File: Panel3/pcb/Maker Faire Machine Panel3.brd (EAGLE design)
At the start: 101.6 x 87.6 mm, 40 parts, among them IC1 TJA1049

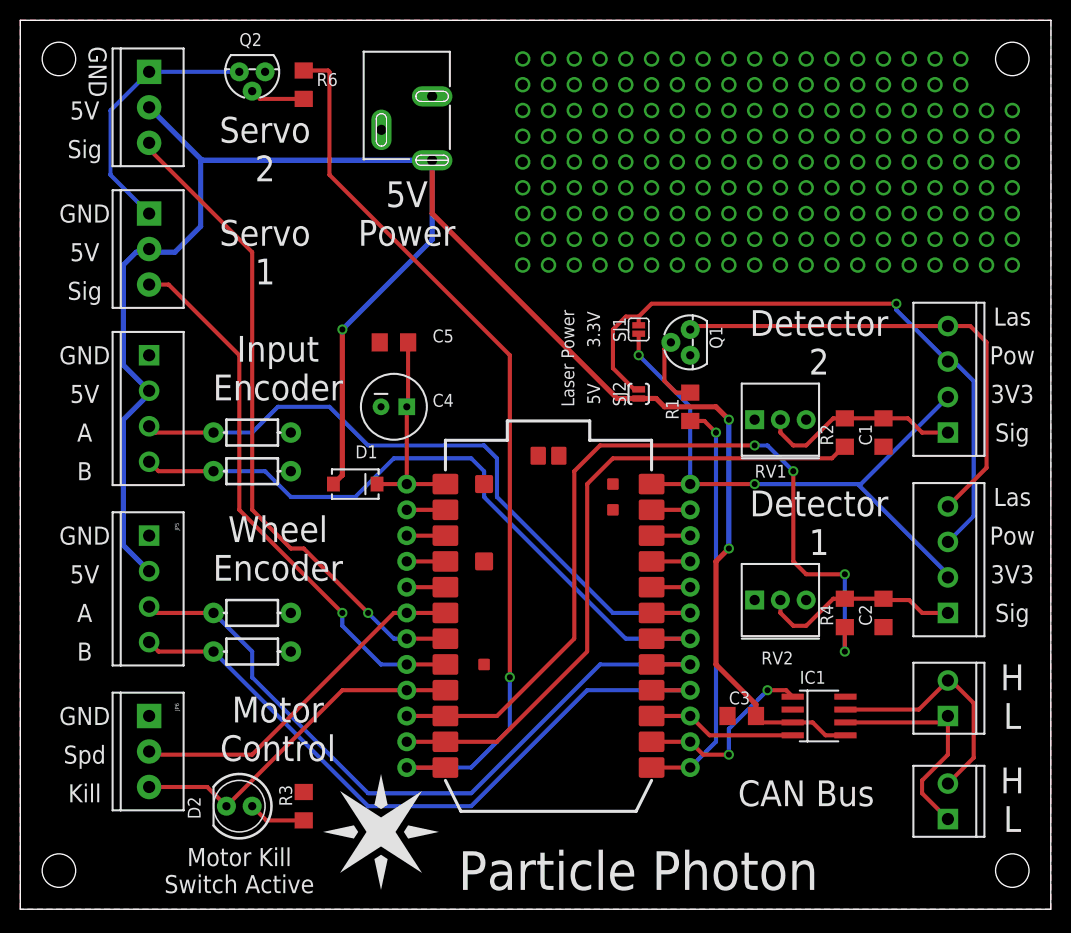
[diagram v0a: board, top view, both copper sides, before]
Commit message: Update Panel 3 PCB after Eric's comments
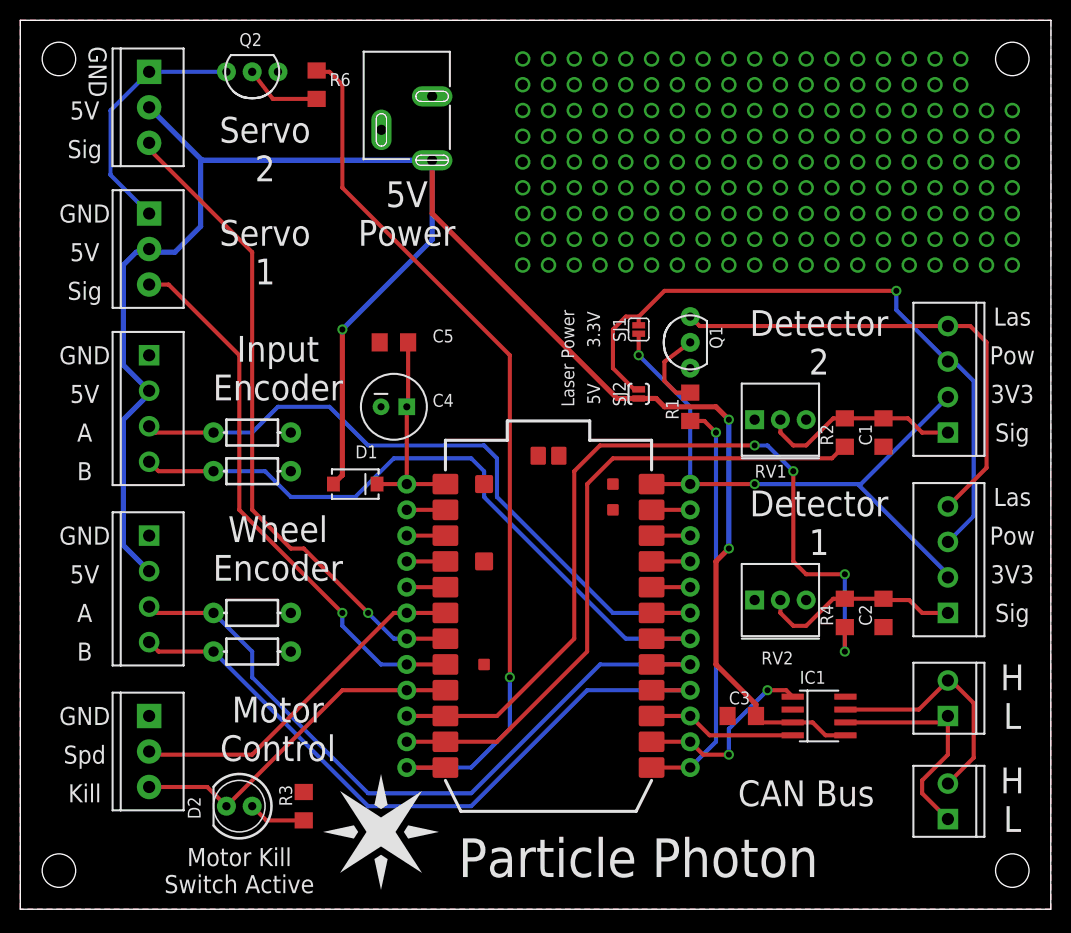
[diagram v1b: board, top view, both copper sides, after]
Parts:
- Q1, Q2: device SparkFun-DiscreteSemi:TO-92 -> SparkFun-DiscreteSemi:TO-92-AMMO
- moved R6 1.27 mm to (30.5, 88.9)
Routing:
- net N$4: track 5.40 -> 7.67 mm
- net LASER_VCC: track 65.1 -> 66.9 mm
- net SERVO_GND: track 26.0 -> 24.7 mm
- net SERVO_EN: track 90.3 -> 89.0 mm
- net N$1: track 7.09 -> 8.09 mm
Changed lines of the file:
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@@
 <vertex x="68.58" y="7.62"/>
 </polygon>
-<text x="44.45" y="11.43" size="3.81" layer="21" align="center-left">Particle Photon</text>
+<text x="44.45" y="12.7" size="3.81" layer="21" align="center-left">Particle Photon</text>
 <text x="78.74" y="19.05" size="2.54" layer="21" align="center">CAN Bus</text>
 <text x="99.06" y="30.48" size="2.54" layer="21" align="center">H</text>
@@
 <attribute name="VALUE" x="91.44" y="35.56" size="0.4064" layer="27" rot="R90"/>
 </element>
-<element name="Q1" library="SparkFun-DiscreteSemi" package="TO-92" value="" x="67.31" y="63.5" smashed="yes" rot="R90">
+<element name="Q1" library="SparkFun-DiscreteSemi" package="TO-92-AMMO" value="" x="67.31" y="63.5" smashed="yes" rot="R90">
 <attribute name="PARTNO" value="PN2222ABU" x="67.31" y="63.5" size="1.778" layer="27" rot="R90" display="off"/>
 <attribute name="NAME" x="70.485" y="62.865" size="1.27" layer="25" ratio="10" rot="R90"/>
@@
 <attribute name="VALUE" x="15.24" y="63.5" size="0.4064" layer="27" rot="R270"/>
 </element>
-<element name="JP5" library="SparkFun-Connectors" package="SCREWTERMINAL-3.5MM-4" value="" x="13.97" y="44.45" rot="R270">
+<element name="JP5" library="SparkFun-Connectors" package="SCREWTERMINAL-3.5MM-4" value="" x="13.97" y="44.45" smashed="yes" rot="R270">
 <attribute name="PARTNO" value="OSTTE030104" x="13.97" y="44.45" size="1.778" layer="27" rot="R270" display="off"/>
-</element>
-<element name="JP6" library="SparkFun-Connectors" package="SCREWTERMINAL-3.5MM-3" value="" x="13.97" y="26.67" rot="R270">
+<attribute name="VALUE" x="15.24" y="45.72" size="0.4064" layer="27" rot="R270"/>
+</element>
+<element name="JP6" library="SparkFun-Connectors" package="SCREWTERMINAL-3.5MM-3" value="" x="13.97" y="26.67" smashed="yes" rot="R270">
 <attribute name="PROD_ID" value="CONN-08288" x="13.97" y="26.67" size="1.778" layer="27" rot="R270" display="off"/>
 <attribute name="PARTNO" value="OSTTE020104" x="13.97" y="26.67" size="1.778" layer="27" rot="R270" display="off"/>
+<attribute name="VALUE" x="15.24" y="27.94" size="0.4064" layer="27" rot="R270"/>
 </element>
 <element name="JP7" library="SparkFun-Connectors" package="POWER_JACK_SLOT" value="POWER_JACKSLT" x="44.45" y="95.25" smashed="yes" rot="R180">
@@
 <attribute name="VALUE" x="15.24" y="91.44" size="0.4064" layer="27" rot="R270"/>
 </element>
-<element name="Q2" library="SparkFun-DiscreteSemi" package="TO-92" value="" x="24.13" y="90.17" smashed="yes" rot="R180">
+<element name="Q2" library="SparkFun-DiscreteSemi" package="TO-92-AMMO" value="" x="24.13" y="90.17" smashed="yes" rot="R180">
 <attribute name="PARTNO" value="PN2222ABU" x="24.13" y="90.17" size="1.778" layer="27" rot="R180" display="off"/>
 <attribute name="NAME" x="22.86" y="92.71" size="1.27" layer="25" ratio="10"/>
 <attribute name="VALUE" x="20.955" y="91.44" size="0.4064" layer="27" ratio="10" rot="R180"/>
 </element>
-<element name="R6" library="SparkFun-Passives" package="1206" value="1k" x="29.21" y="88.9" smashed="yes" rot="R270">
-<attribute name="PARTNO" value="ERJ-8ENF1001V" x="29.21" y="88.9" size="1.778" layer="27" rot="R270" display="off"/>
-<attribute name="NAME" x="30.48" y="88.773" size="1.27" layer="25"/>
-<attribute name="VALUE" x="27.686" y="90.297" size="0.4064" layer="27" rot="R270"/>
+<element name="R6" library="SparkFun-Passives" package="1206" value="1k" x="30.48" y="88.9" smashed="yes" rot="R270">
+<attribute name="PARTNO" value="ERJ-8ENF1001V" x="30.48" y="88.9" size="1.778" layer="27" rot="R270" display="off"/>
+<attribute name="NAME" x="31.75" y="88.773" size="1.27" layer="25"/>
+<attribute name="VALUE" x="28.956" y="90.297" size="0.4064" layer="27" rot="R270"/>
 </element>
 <element name="D2" library="SparkFun-LED" package="LED5MM" value="" x="22.86" y="17.78" smashed="yes" rot="R180">
@@
 <wire x1="67.31" y1="58.55" x2="65.91" y2="58.55" width="0.4064" layer="1"/>
 <wire x1="65.91" y1="58.55" x2="64.77" y2="59.69" width="0.4064" layer="1"/>
-<wire x1="64.77" y1="59.69" x2="64.77" y2="62.865" width="0.4064" layer="1"/>
-<wire x1="64.77" y1="62.865" x2="65.405" y2="63.5" width="0.4064" layer="1"/>
+<wire x1="64.77" y1="59.69" x2="64.77" y2="61.595" width="0.4064" layer="1"/>
+<wire x1="64.77" y1="61.595" x2="67.31" y2="63.5" width="0.4064" layer="1"/>
 </signal>
 <signal name="LASER_GND">
@@
 <contactref element="JP1" pad="4"/>
 <contactref element="JP2" pad="4"/>
-<wire x1="92.71" y1="65.11" x2="67.65" y2="65.11" width="0.4064" layer="1"/>
-<wire x1="67.65" y1="65.11" x2="67.31" y2="64.77" width="0.4064" layer="1"/>
 <wire x1="92.71" y1="65.11" x2="94.91" y2="65.11" width="0.4064" layer="1"/>
 <wire x1="94.91" y1="65.11" x2="96.52" y2="63.5" width="0.4064" layer="1"/>
 <wire x1="96.52" y1="63.5" x2="96.52" y2="51.14" width="0.4064" layer="1"/>
 <wire x1="96.52" y1="51.14" x2="92.71" y2="47.33" width="0.4064" layer="1"/>
+<wire x1="92.71" y1="65.11" x2="68.24" y2="65.11" width="0.4064" layer="1"/>
+<wire x1="68.24" y1="65.11" x2="67.31" y2="66.04" width="0.4064" layer="1"/>
 </signal>
 <signal name="SERVO_EN">
@@
 <contactref element="JP11" pad="1"/>
 <wire x1="43.18" y1="21.59" x2="39.37" y2="21.59" width="0.4064" layer="1"/>
-<wire x1="29.21" y1="90.3" x2="31.62" y2="90.3" width="0.4064" layer="1"/>
-<wire x1="31.62" y1="90.3" x2="31.75" y2="90.17" width="0.4064" layer="1"/>
-<wire x1="31.75" y1="90.17" x2="31.75" y2="80.01" width="0.4064" layer="1"/>
-<wire x1="31.75" y1="80.01" x2="49.53" y2="62.23" width="0.4064" layer="1"/>
+<wire x1="33.02" y1="78.74" x2="49.53" y2="62.23" width="0.4064" layer="1"/>
 <wire x1="49.53" y1="62.23" x2="49.53" y2="30.48" width="0.4064" layer="1"/>
 <via x="49.53" y="30.48" extent="1-16" drill="0.6"/>
@@
 <wire x1="49.53" y1="25.4" x2="45.72" y2="21.59" width="0.4064" layer="16"/>
 <wire x1="45.72" y1="21.59" x2="39.37" y2="21.59" width="0.4064" layer="16"/>
+<wire x1="33.02" y1="78.74" x2="33.02" y2="88.9" width="0.4064" layer="1"/>
+<wire x1="33.02" y1="88.9" x2="31.75" y2="90.17" width="0.4064" layer="1"/>
+<wire x1="31.75" y1="90.17" x2="30.61" y2="90.17" width="0.4064" layer="1"/>
+<wire x1="30.61" y1="90.17" x2="30.48" y2="90.3" width="0.4064" layer="1"/>
 </signal>
 <signal name="5V">
@@
 <wire x1="60.96" y1="66.04" x2="62.23" y2="66.04" width="0.4064" layer="1"/>
 <wire x1="62.23" y1="65.1819" x2="62.23" y2="66.04" width="0.4064" layer="1"/>
-<wire x1="62.23" y1="66.04" x2="63.5" y2="67.31" width="0.4064" layer="1"/>
-<wire x1="63.5" y1="67.31" x2="87.63" y2="67.31" width="0.4064" layer="1"/>
-<via x="87.63" y="67.31" extent="1-16" drill="0.6"/>
-<wire x1="87.63" y1="67.31" x2="87.63" y2="66.69" width="0.4064" layer="16"/>
+<wire x1="62.23" y1="66.04" x2="64.77" y2="68.58" width="0.4064" layer="1"/>
+<wire x1="64.77" y1="68.58" x2="87.63" y2="68.58" width="0.4064" layer="1"/>
+<via x="87.63" y="68.58" extent="1-16" drill="0.6"/>
+<wire x1="87.63" y1="68.58" x2="87.63" y2="66.69" width="0.4064" layer="16"/>
 <wire x1="87.63" y1="66.69" x2="92.71" y2="61.61" width="0.4064" layer="16"/>
 <wire x1="92.71" y1="61.61" x2="93.33" y2="61.61" width="0.4064" layer="16"/>
@@
 <wire x1="10.16" y1="80.01" x2="13.97" y2="76.2" width="0.4064" layer="16"/>
 <wire x1="13.97" y1="90.17" x2="10.16" y2="86.36" width="0.4064" layer="16"/>
-<wire x1="13.97" y1="90.17" x2="22.86" y2="90.17" width="0.4064" layer="16"/>
+<wire x1="13.97" y1="90.17" x2="21.59" y2="90.17" width="0.4064" layer="16"/>
 </signal>
 <signal name="N$4">
 <contactref element="R6" pad="2"/>
 <contactref element="Q2" pad="2"/>
-<wire x1="29.21" y1="87.5" x2="24.895" y2="87.5" width="0.4064" layer="1"/>
-<wire x1="24.895" y1="87.5" x2="24.13" y2="88.265" width="0.4064" layer="1"/>
+<wire x1="30.48" y1="87.5" x2="26.165" y2="87.5" width="0.4064" layer="1"/>
+<wire x1="26.165" y1="87.5" x2="24.13" y2="90.17" width="0.4064" layer="1"/>
 </signal>
 <signal name="LASER_EN">

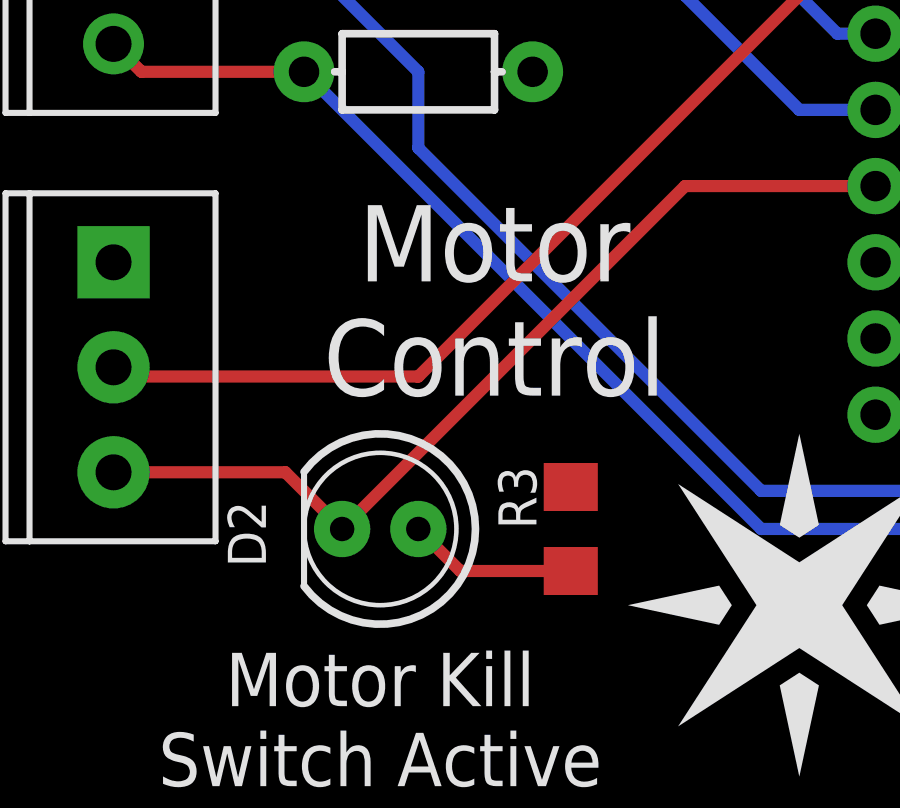
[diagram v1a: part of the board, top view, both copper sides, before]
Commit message: Fix LED orientation
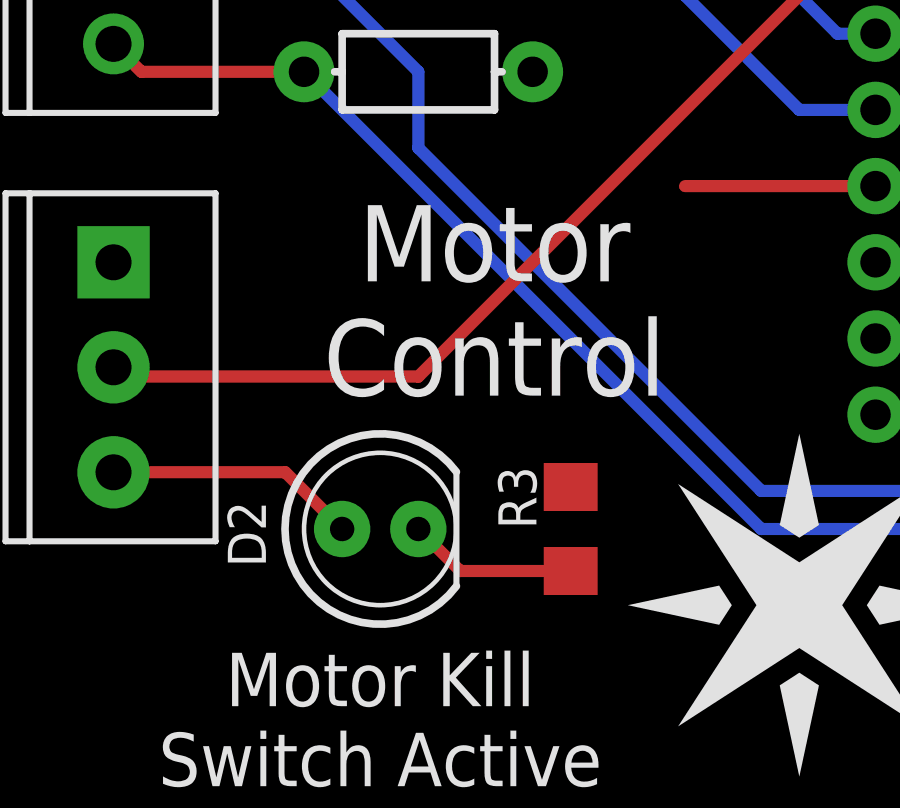
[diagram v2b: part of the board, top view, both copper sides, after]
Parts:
- turned D2 to 0 degrees
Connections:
- net MOTOR_KILL: now also D2.A; no longer D2.K
- net N$5: now also D2.K; no longer D2.A
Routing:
- net MOTOR_KILL: track 34.7 -> 18.6 mm
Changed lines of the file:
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@@
 <attribute name="VALUE" x="28.956" y="90.297" size="0.4064" layer="27" rot="R270"/>
-</element>
-<element name="D2" library="SparkFun-LED" package="LED5MM" value="" x="22.86" y="17.78" smashed="yes" rot="R180">
-<attribute name="PARTNO" value="SSL-LX5093HD" x="22.86" y="17.78" size="1.778" layer="27" rot="R180" display="off"/>
-<attribute name="NAME" x="19.05" y="16.51" size="1.27" layer="25" ratio="10" rot="R90"/>
-<attribute name="VALUE" x="19.6596" y="19.5834" size="1.27" layer="27" ratio="10" rot="R180"/>
 </element>
 <element name="RV1" library="SparkFun-Electromechanical" package="3362U" value="2k" x="73.66" y="53.34" smashed="yes">
@@
 <attribute name="BOM" value="EXCLUDE" x="24.13" y="36.83" size="1.778" layer="27" rot="R180" display="off"/>
 <attribute name="VALUE" x="26.289" y="37.592" size="1.27" layer="21" font="vector" ratio="15" rot="R180"/>
+</element>
+<element name="D2" library="SparkFun-LED" package="LED5MM" value="" x="22.86" y="17.78" smashed="yes">
+<attribute name="PARTNO" value="SSL-LX5093HD" x="22.86" y="17.78" size="1.778" layer="27" display="off"/>
+<attribute name="NAME" x="19.05" y="16.51" size="1.27" layer="25" rot="R90"/>
+<attribute name="VALUE" x="26.0604" y="15.9766" size="1.27" layer="27" ratio="10"/>
 </element>
 </elements>
@@
 <signal name="MOTOR_KILL">
 <contactref element="JP6" pad="3"/>
-<contactref element="D2" pad="K"/>
 <contactref element="U$1" pad="9"/>
-<wire x1="21.59" y1="17.78" x2="33.02" y2="29.21" width="0.4064" layer="1"/>
 <wire x1="33.02" y1="29.21" x2="43.18" y2="29.21" width="0.4064" layer="1"/>
-<wire x1="21.59" y1="17.78" x2="19.7" y2="19.67" width="0.4064" layer="1"/>
 <wire x1="19.7" y1="19.67" x2="13.97" y2="19.67" width="0.4064" layer="1"/>
 <contactref element="JP11" pad="4"/>
+<contactref element="D2" pad="A"/>
+<wire x1="21.59" y1="17.78" x2="19.7" y2="19.67" width="0.4064" layer="1"/>
 <wire x1="43.18" y1="29.21" x2="39.37" y2="29.21" width="0" layer="19" extent="1-1"/>
+<wire x1="21.59" y1="17.78" x2="33.02" y2="29.21" width="0" layer="19" extent="1-1"/>
 </signal>
 <signal name="SERVO_2">
@@
 </signal>
 <signal name="N$5">
-<contactref element="D2" pad="A"/>
 <contactref element="R3" pad="2"/>
+<wire x1="25.53" y1="16.38" x2="29.21" y2="16.38" width="0.4064" layer="1"/>
+<contactref element="D2" pad="K"/>
 <wire x1="24.13" y1="17.78" x2="25.53" y2="16.38" width="0.4064" layer="1"/>
-<wire x1="25.53" y1="16.38" x2="29.21" y2="16.38" width="0.4064" layer="1"/>
 </signal>
 <signal name="WKP">
